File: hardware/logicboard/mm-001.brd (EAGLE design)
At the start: 47 x 47 mm, 21 parts, among them IC1 74ALS05N, IC2 LTC485N, IC3 LTC485N

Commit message: Rebuild.
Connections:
- net RX+: now also JP2.5; no longer JP2.7
- net RX-: now also JP2.6; no longer JP2.8
- net TX+: now also JP2.7; no longer JP2.5
- net TX-: now also JP2.8; no longer JP2.6
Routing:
- net GND: track 145.1 -> 130.0 mm, vias 0 -> 1
- net VCC: track 126.0 -> 138.3 mm
- net RX-: track 24.1 -> 16.4 mm
- net RX+: track 25.3 -> 17.8 mm
- net NMIDIOUT: track 45.7 -> 51.7 mm, vias 1 -> 0
- net LED: track 38.7 -> 32.9 mm
- net V+: track 49.3 -> 54.6 mm
- net TX-: track 13.3 -> 11.3 mm
- net MIDIIN: track 13.6 -> 12.9 mm

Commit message: Finish up.
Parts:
- moved RN1 1.50 mm to (5.50, 31.0)
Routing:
- net VCC: track 138.3 -> 121.5 mm
- net NMIDIOUT: track 51.7 -> 61.9 mm
- net V+: track 54.6 -> 50.9 mm
- net MIDIOUT: track 15.2 -> 18.4 mm
- net MOSND: track 29.5 -> 32.5 mm
- net MORTN: track 29.7 -> 31.5 mm
- net TX: track 36.6 -> 35.2 mm
- net MIRTN: track 22.4 -> 23.6 mm
- net RX+: track 17.8 -> 19.0 mm
- net MIDIIN: track 12.9 -> 13.9 mm
- net GND: track 130.0 -> 129.5 mm, vias 1 -> 2

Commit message: Added test leds.
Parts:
- added LED1, LED2: (no value), led:LED3MM
- added R7, R8: 1k, rcl:0204/5
- moved LOGO1 16.8 mm to (23.5, 9.50)
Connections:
- removed net MIDIOUT: IC1.10, R3.2
- removed net RX: IC1.9, IC2.1
- new net LED1: IC1.6, R7.2
- new net LED1K: LED1.K, R7.1
- new net LED2: IC1.10, R8.2
- new net LED2K: LED2.K, R8.1
- new net N$1: IC1.1, IC2.1
- new net N$2: IC1.4, R3.2
- new net N$5: IC1.11, IC1.8, RN1.4
- net GND: no longer IC1.1, IC1.3, IC1.5
- net NMIDIOUT: now also IC1.2, IC1.3, IC1.5; no longer IC1.11, IC1.8
- net TX: now also IC1.9
- net VCC: now also LED1.A, LED2.A
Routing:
- net VCC: track 121.5 -> 190.0 mm
- net N$5: track 0.00 -> 57.4 mm
- net LED2: track 0.00 -> 40.8 mm
- net RX: track 30.0 -> 0.00 mm
- net N$2: track 0.00 -> 23.9 mm, vias 0 -> 1
- net N$1: track 0.00 -> 22.6 mm
- net MIDIOUT: track 18.4 -> 0.00 mm
- net NMIDIOUT: track 61.9 -> 48.3 mm
- net TX: track 35.2 -> 46.8 mm, vias 0 -> 1
- net LED1: track 0.00 -> 6.29 mm
- net LED2K: track 0.00 -> 5.26 mm
- net LED1K: track 0.00 -> 5.26 mm
- net MOSND: track 32.5 -> 29.5 mm
- net MORTN: track 31.5 -> 29.7 mm
- net V+: track 50.9 -> 49.7 mm
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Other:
- board text added: "+"
- board text added: "MIDI IN"
- board text added: "MIDI RECV"

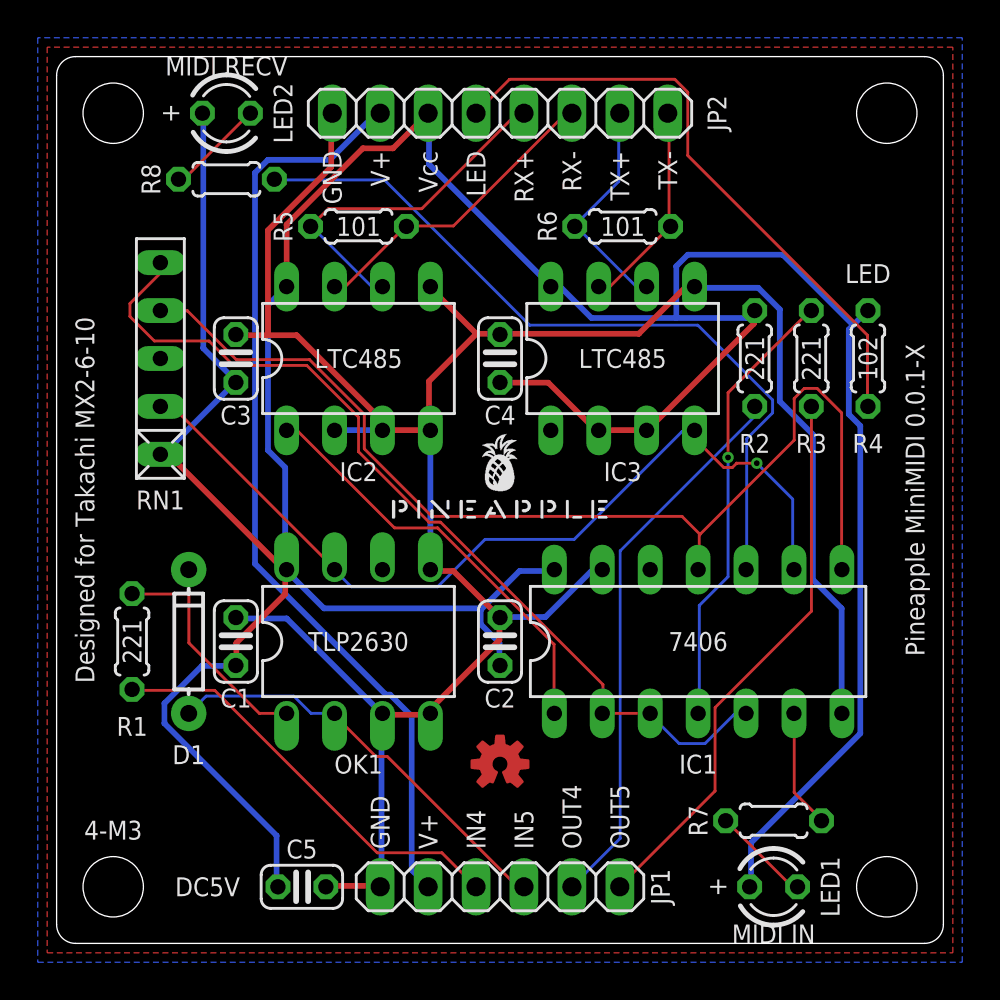
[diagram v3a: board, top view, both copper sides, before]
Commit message: TX+/TX-/GND, RX+/RX-/GND.
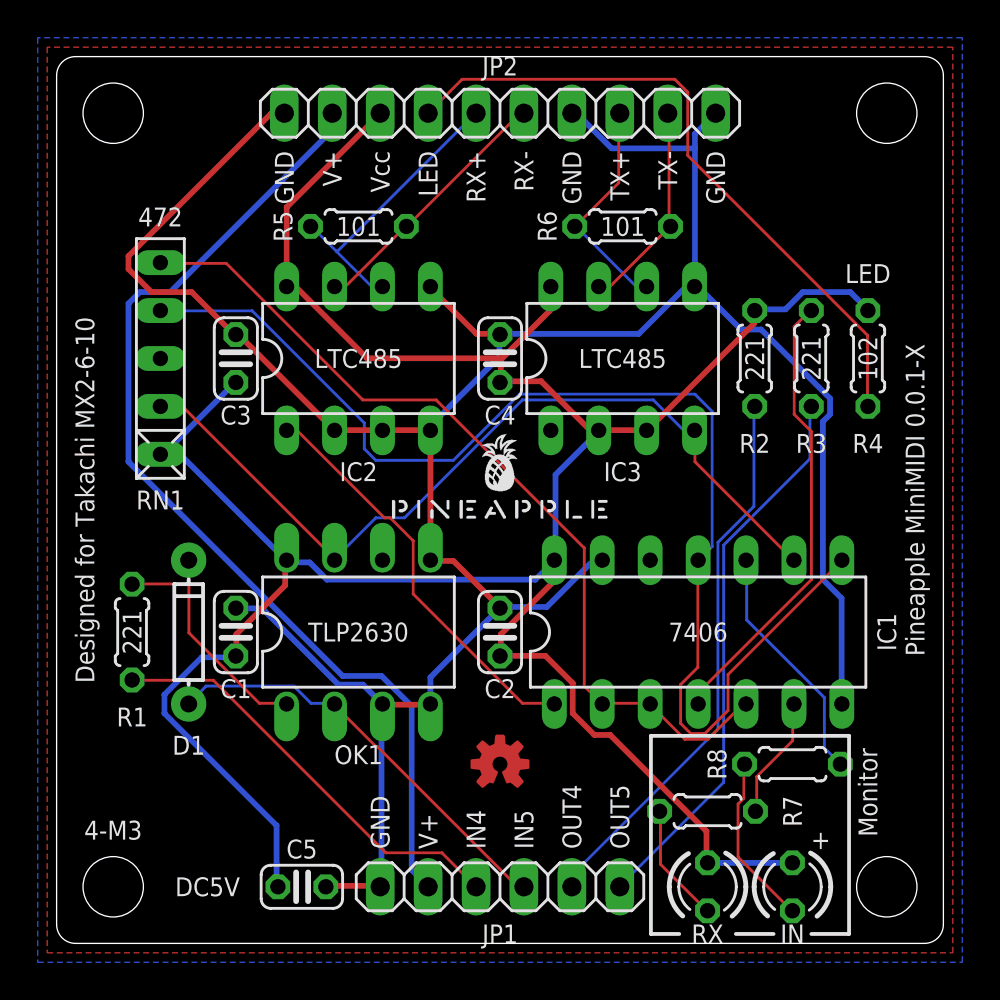
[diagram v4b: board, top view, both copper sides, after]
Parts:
- removed LED1, LED2: (no value), led:LED3MM
- added IN: MIDIIN, led:LED3MM
- added RX: MIDIRX, led:LED3MM
- JP2: device pinhead:1X08 -> pinhead:1X10
- moved R8 43.1 mm to (39.0, 9.50)
- moved R7 3.54 mm to (34.5, 7.00)
- moved C1 0.50 mm to (9.50, 16.5)
- moved C2 0.50 mm to (23.5, 16.5)
- moved D1 0.50 mm to (7.00, 16.5)
- moved IC1 0.50 mm to (34.0, 16.5)
- moved OK1 0.50 mm to (16.0, 16.5)
- moved R1 0.50 mm to (4.00, 16.5)
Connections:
- net GND: now also JP2.10, JP2.7
- net LED1K: now also RX.K; no longer LED1.K
- net LED2K: now also IN.K; no longer LED2.K
- net TX+: now also JP2.8; no longer JP2.7
- net TX-: now also JP2.9; no longer JP2.8
- net VCC: now also IN.A, RX.A; no longer LED1.A, LED2.A
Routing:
- net VCC: track 190.0 -> 144.4 mm
- net LED2: track 40.8 -> 12.9 mm
- net GND: track 128.5 -> 147.6 mm
- net N$5: track 57.4 -> 66.1 mm
- net V+: track 49.7 -> 54.2 mm
- net LED2K: track 5.26 -> 9.12 mm
- net RX+: track 19.0 -> 15.6 mm
- net LED: track 32.9 -> 35.4 mm
- net RX-: track 16.4 -> 13.9 mm
- net TX: track 46.8 -> 45.1 mm, vias 1 -> 0
- net NMIDIOUT: track 48.3 -> 46.6 mm
- net LED1K: track 5.26 -> 6.33 mm
- net N$1: track 22.6 -> 21.9 mm
- net N$2: track 23.9 -> 24.1 mm, vias 1 -> 0
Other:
- board text added: "472"
- board text added: "Monitor"
- board text removed: "MIDI IN"
- board text removed: "MIDI RECV"

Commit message: Changed positions of the monitor leds.
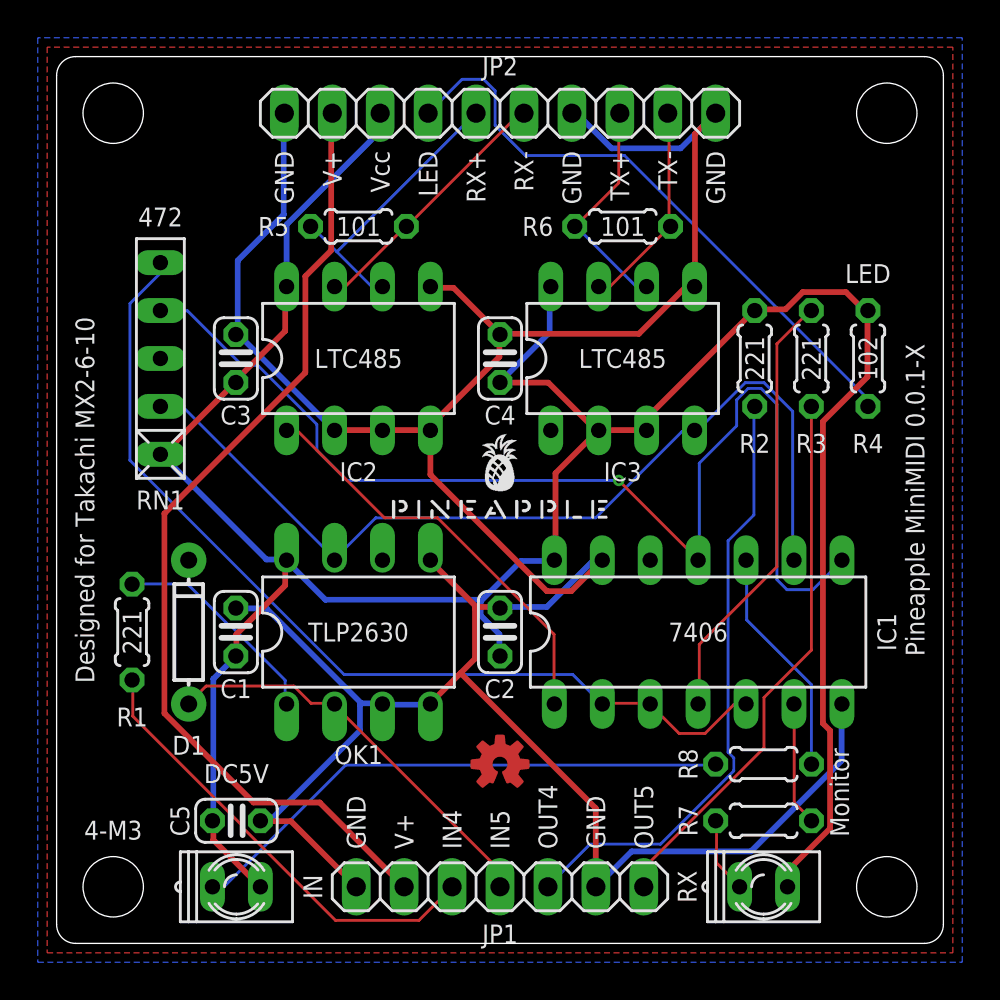
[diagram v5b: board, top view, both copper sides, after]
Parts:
- IN, RX: device led:LED3MM -> led:Q62902-B152
- JP1: device pinhead:1X06 -> pinhead:1X07
- moved IN 29.5 mm to (9.53, 3.00), turned to 0 degrees
- moved C5 4.93 mm to (9.53, 6.50)
- moved R7 3.01 mm to (37.5, 6.50)
- moved RX 2.97 mm to (37.5, 3.00), turned to 0 degrees
- moved R8 1.53 mm to (37.5, 9.50)
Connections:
- net GND: now also JP1.6
- net MORTN: now also JP1.7; no longer JP1.6
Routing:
- net LED2K: track 9.12 -> 29.4 mm
- net GND: track 147.6 -> 159.7 mm
- net N$5: track 66.1 -> 60.5 mm, vias 0 -> 1
- net TX: track 45.1 -> 49.5 mm
- net NMIDIOUT: track 46.6 -> 50.5 mm
- net MOSND: track 29.5 -> 32.4 mm
- net LED: track 35.4 -> 32.5 mm
- net LED1K: track 6.33 -> 4.03 mm
- net V+: track 54.2 -> 52.0 mm
- net VCC: track 144.4 -> 142.5 mm
- net MISND: track 22.8 -> 24.1 mm
- net MIRTN: track 22.7 -> 21.9 mm
- net MIDIIN: track 13.6 -> 12.8 mm
- net N$2: track 24.1 -> 23.4 mm
- net LED2: track 12.9 -> 12.2 mm
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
